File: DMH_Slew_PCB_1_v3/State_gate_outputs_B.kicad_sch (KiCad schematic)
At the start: 26 parts, among them J10 TS_Jack_6.35mm_Sw, J61 Conn_01x08_PinHeader, J9 TS_Jack_6.35mm_Sw, Q11 BC548, Q12 BC548, U3 TL074

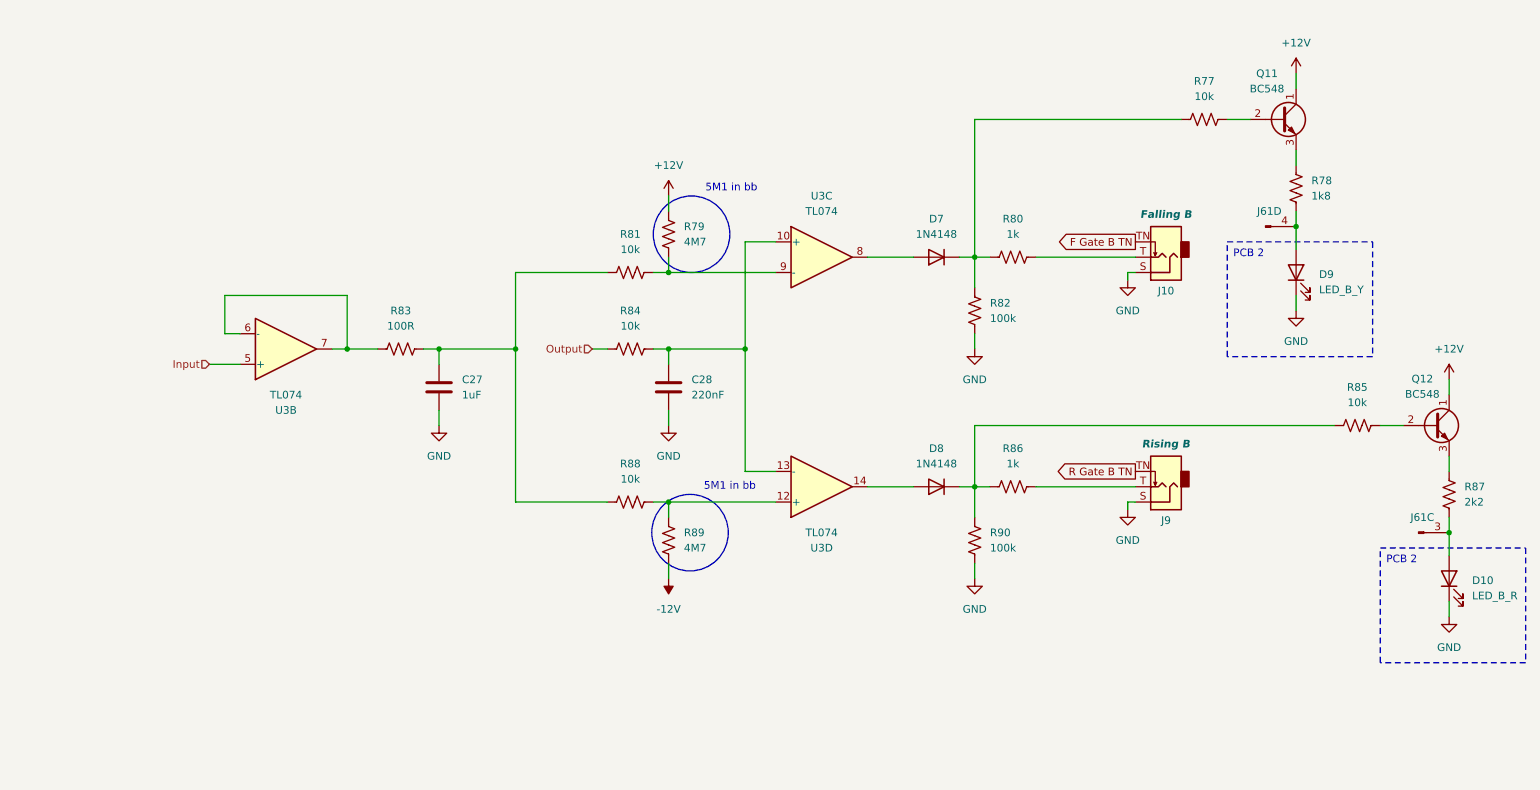
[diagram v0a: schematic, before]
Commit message: V3 sch redesign ongoing
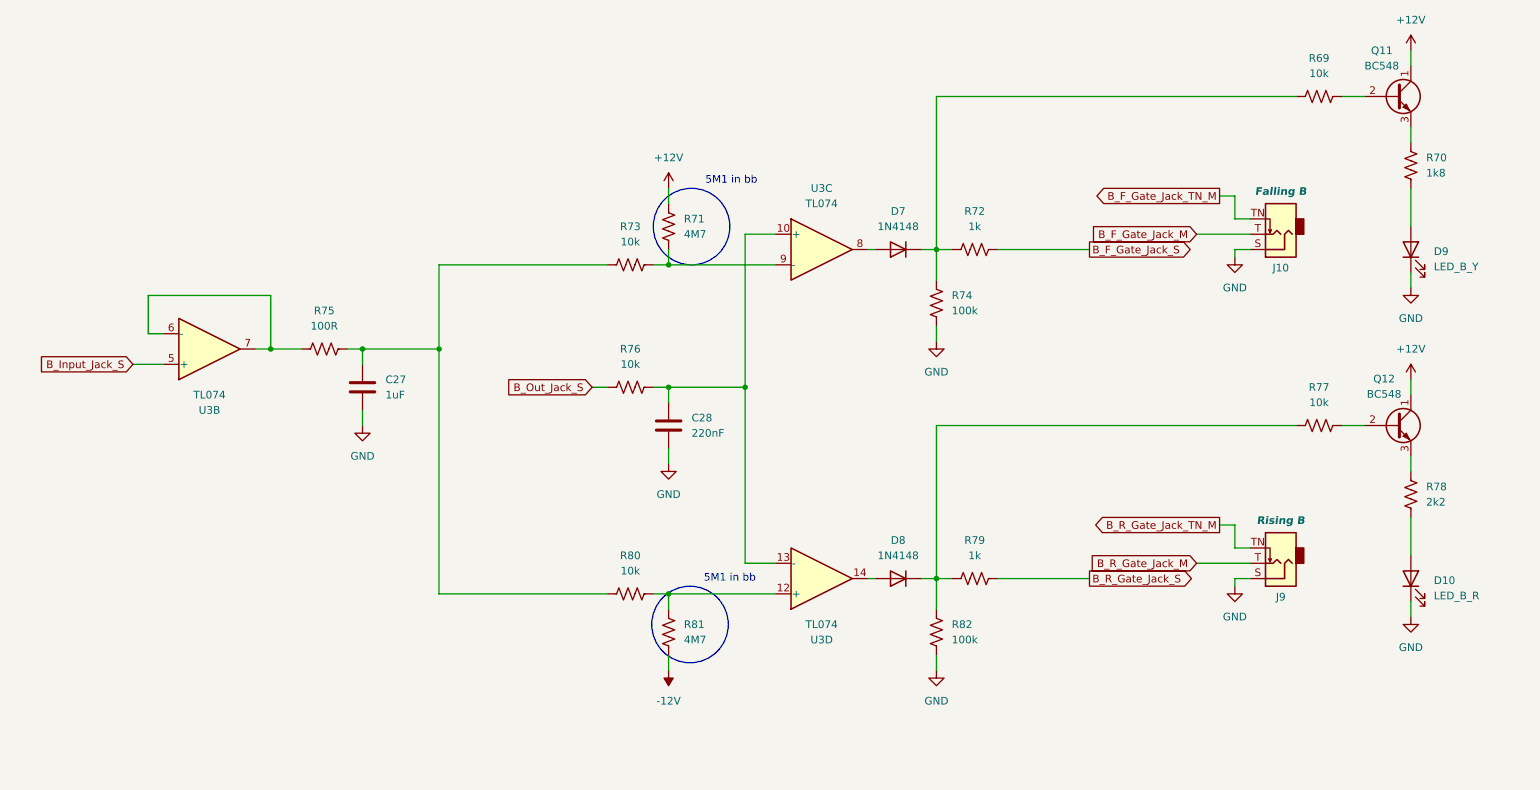
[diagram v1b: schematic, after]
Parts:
- removed J61: Conn_01x08_PinHeader, Connector_PinHeader_2.54mm:PinHeader_1x08_P2.54mm_Vertical, symbol SynthStuff:Conn_01x08_PinHeader
- removed R83: 100R, Resistor_THT:R_Axial_DIN0207_L6.3mm_D2.5mm_P7.62mm_Horizontal, symbol Device:R_US
- removed R84, R85, R88: 10k, Resistor_THT:R_Axial_DIN0207_L6.3mm_D2.5mm_P7.62mm_Horizontal, symbol Device:R_US
- removed R86: 1k, Resistor_THT:R_Axial_DIN0207_L6.3mm_D2.5mm_P7.62mm_Horizontal, symbol Device:R_US
- removed R87: 2k2, Resistor_THT:R_Axial_DIN0207_L6.3mm_D2.5mm_P7.62mm_Horizontal, symbol Device:R_US
- removed R89: 4M7, Resistor_THT:R_Axial_DIN0207_L6.3mm_D2.5mm_P7.62mm_Horizontal, symbol Device:R_US
- removed R90: 100k, Resistor_THT:R_Axial_DIN0207_L6.3mm_D2.5mm_P7.62mm_Horizontal, symbol Device:R_US
- added R69, R73, R76: 10k, Resistor_THT:R_Axial_DIN0207_L6.3mm_D2.5mm_P7.62mm_Horizontal, symbol Device:R_US
- added R70: 1k8, Resistor_THT:R_Axial_DIN0207_L6.3mm_D2.5mm_P7.62mm_Horizontal, symbol Device:R_US
- added R71: 4M7, Resistor_THT:R_Axial_DIN0207_L6.3mm_D2.5mm_P7.62mm_Horizontal, symbol Device:R_US
- added R72: 1k, Resistor_THT:R_Axial_DIN0207_L6.3mm_D2.5mm_P7.62mm_Horizontal, symbol Device:R_US
- added R74: 100k, Resistor_THT:R_Axial_DIN0207_L6.3mm_D2.5mm_P7.62mm_Horizontal, symbol Device:R_US
- added R75: 100R, Resistor_THT:R_Axial_DIN0207_L6.3mm_D2.5mm_P7.62mm_Horizontal, symbol Device:R_US
- R78: value 1k8 -> 2k2
- R79: value 4M7 -> 1k
- R80: value 1k -> 10k
- R81: value 10k -> 4M7
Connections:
- net +12V: now also R71.1; no longer R79.1
- net -12V: now also R81.2
- net GND: now also R74.2
- net at Q12.2 (B): now also R77.1
- net at D8.1 (K): now also R77.2, R79.2, R82.1
- net at D10.2 (A): now also R78.2
- net at R80.1: now also R81.1, U3.12 (+); no longer J10.T
- net at Q11.2 (B): now also R69.1; no longer R77.1
- net at R78.1: now also Q12.3 (E); no longer Q11.3 (E)
- net at C28.1, U3.10 (+), U3.13 (-): now also R76.1
- net at D9.2 (A): now also R70.2; no longer R78.2
- net B_R_Gate_Jack_M: now reaches J9.T
- net at C27.1: now also R80.2, R73.2, R75.1; no longer R81.2
- net at U3.6 (-), U3.7: now also R75.2
- net F Gate B TN renamed B_F_Gate_Jack_TN_M
- net Input renamed B_Input_Jack_S
- net R Gate B TN renamed B_R_Gate_Jack_TN_M
- new net: D7.1 (K), R69.2, R72.2, R74.1
- new net: R71.2, R73.1, U3.9 (-)
- new net: Q11.3 (E), R70.1
- new net B_F_Gate_Jack_M: J10.T
- new net B_F_Gate_Jack_S: R72.1
- new net B_Out_Jack_S: R76.2
- new net B_R_Gate_Jack_S: R79.1
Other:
- note removed: "PCB 2"

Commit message: Finished PCB1 v3 schematic
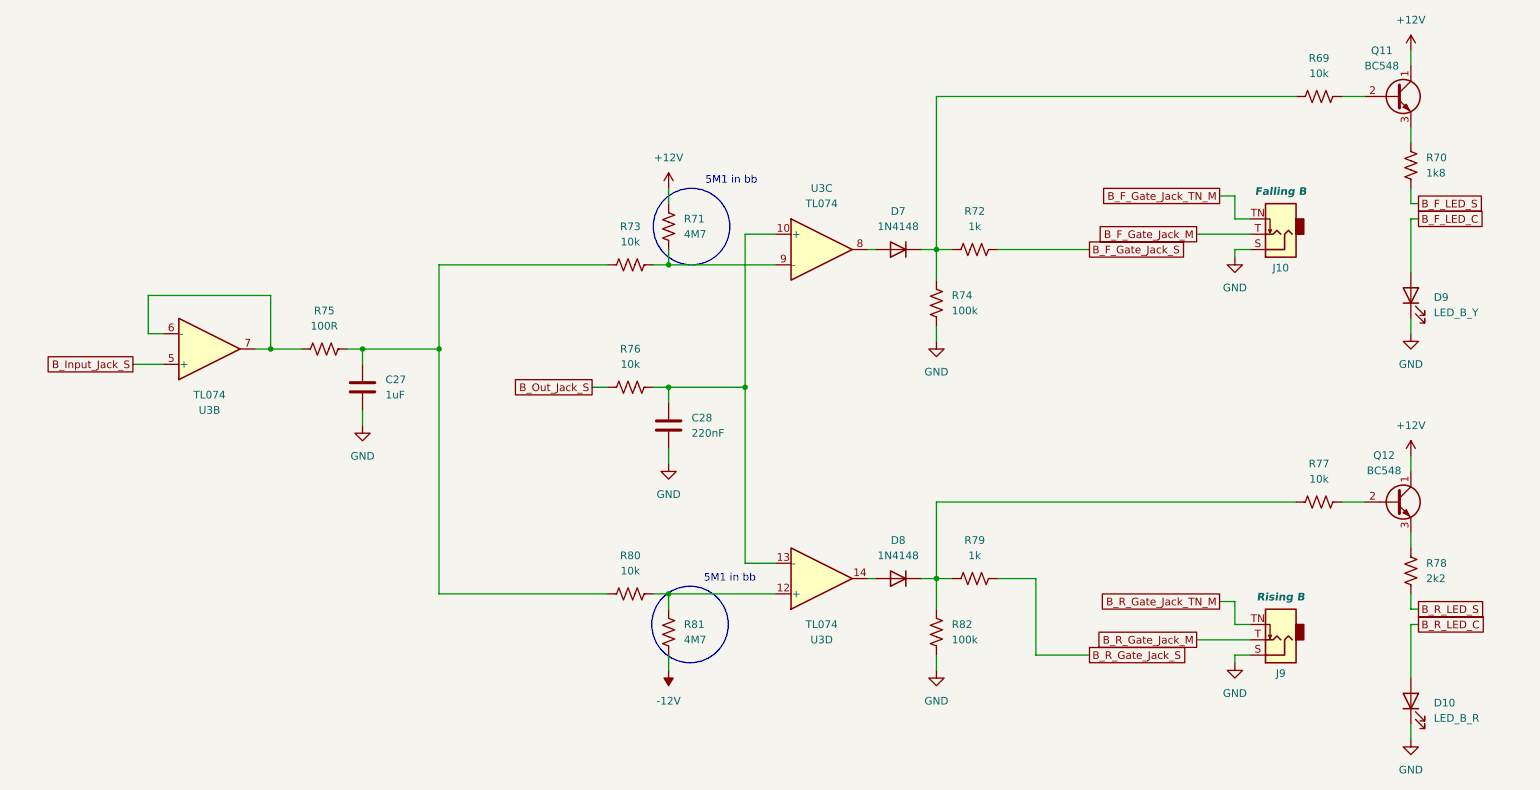
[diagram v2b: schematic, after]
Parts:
- Q11, Q12: footprint Package_TO_SOT_THT:TO-92L_Inline_Wide -> Package_TO_SOT_THT:TO-92_Inline
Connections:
- net B_R_LED_C: now reaches D10.2 (A)
- net B_R_LED_C: no longer R78.2
- net B_F_LED_C: now reaches D9.2 (A)
- net B_F_LED_C: no longer R70.2
- new net B_F_LED_S: R70.2
- new net B_R_LED_S: R78.2
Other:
- moved on the sheet: D10, D9, J9, Q12, R77, R78

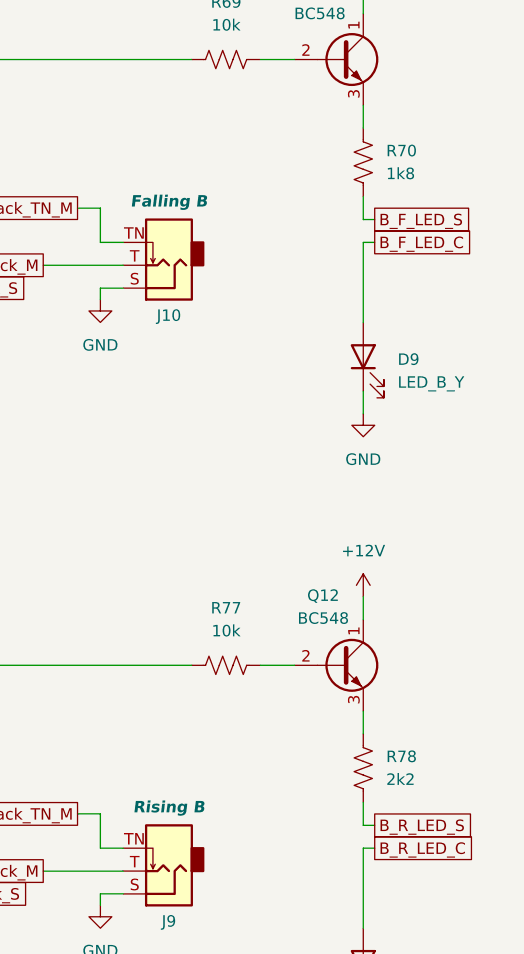
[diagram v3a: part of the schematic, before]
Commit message: Corrected PCB 2 switch positions
and Regenerated Gerbers
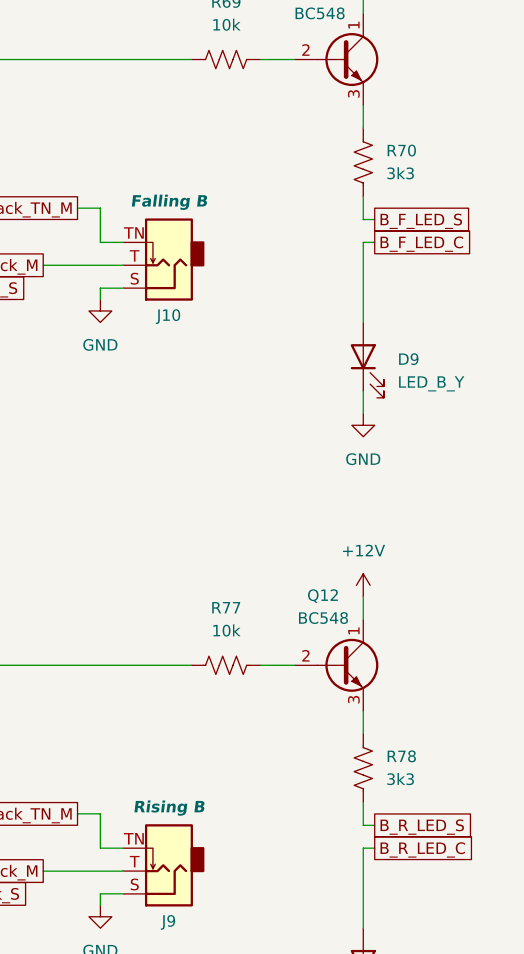
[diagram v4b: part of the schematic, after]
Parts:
- R70: value 1k8 -> 3k3
- R78: value 2k2 -> 3k3
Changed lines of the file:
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@@
 			)
 		)
-		(property "Value" "2k2"
+		(property "Value" "3k3"
 			(at 252.73 114.2999 0)
 			(effects
@@
 			)
 		)
-		(property "Value" "1k8"
+		(property "Value" "3k3"
 			(at 252.73 46.9899 0)
 			(effects

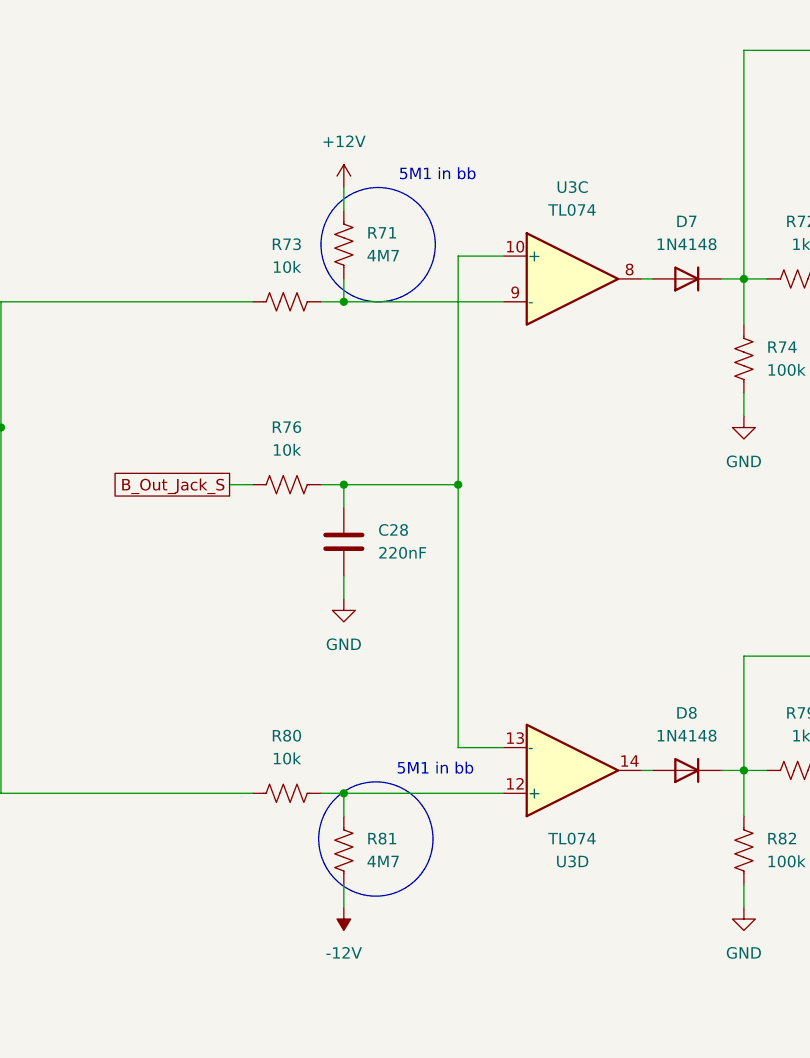
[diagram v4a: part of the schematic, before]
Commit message: Redesigned Main PCB
and regenerated Gerbers
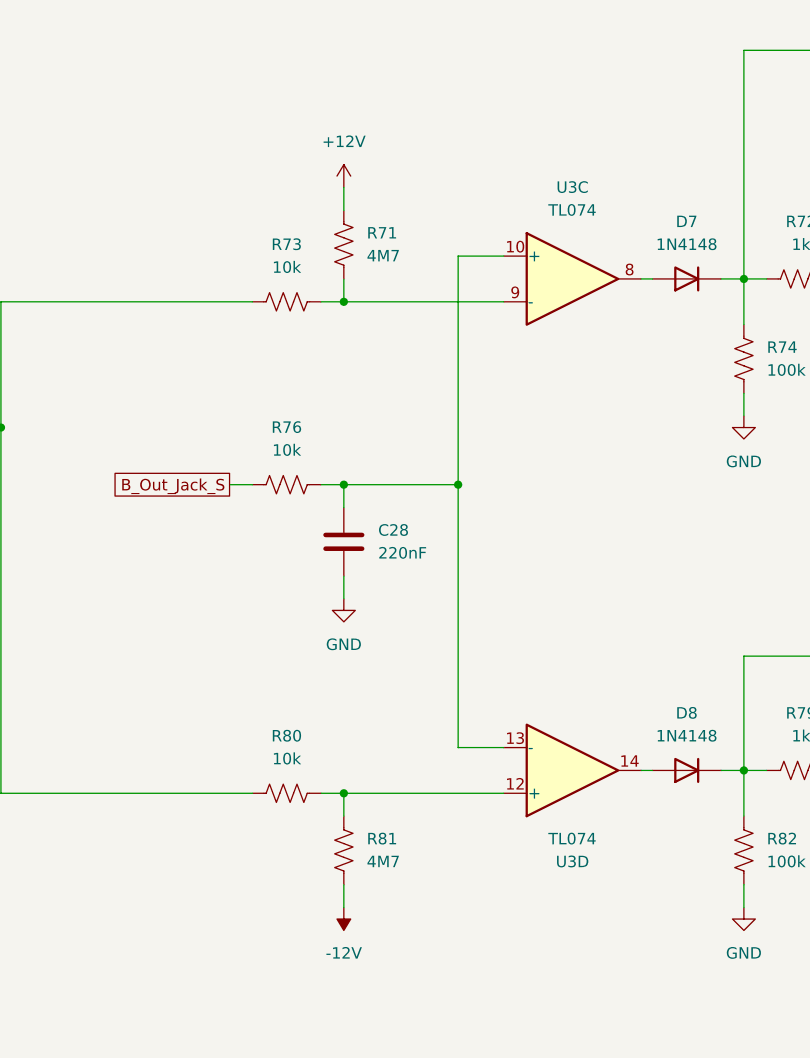
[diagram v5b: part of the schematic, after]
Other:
- note removed: "5M1 in bb"
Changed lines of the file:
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@@
 		(comment 1 "PCB for 5 cm Kosmo format synthesizer module")
-	)
-	(circle
-		(center 130.556 121.92)
-		(radius 6.35)
-		(stroke
-			(width 0)
-			(type default)
-		)
-		(fill
-			(type none)
-		)
-	)
-	(circle
-		(center 130.81 55.88)
-		(radius 6.35)
-		(stroke
-			(width 0)
-			(type default)
-		)
-		(fill
-			(type none)
-		)
-	)
-	(text "5M1 in bb"
-		(exclude_from_sim no)
-		(at 137.414 48.26 0)
-		(effects
-			(font
-				(size 1.27 1.27)
-			)
-		)
-	)
-	(text "5M1 in bb"
-		(exclude_from_sim no)
-		(at 137.16 114.3 0)
-		(effects
-			(font
-				(size 1.27 1.27)
-			)
-		)
 	)
 	(junction
